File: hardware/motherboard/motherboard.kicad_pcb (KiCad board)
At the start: 2 copper layers, 175 x 127 mm, 82 parts, among them J1 Conn_01x04_Female, J10 Conn_01x02_Female, J11 Conn_01x02_Female, J12 Conn_01x03_Male, J13 Conn_01x03_Male, J14 Conn_01x03_Male, J15 Conn_01x06_Female, J16 Conn_01x02_Female, J2 Conn_01x03_Male, J3 Conn_01x05_Female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

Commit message: version v0.3
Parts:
- removed D10: LED, LED_SMD:LED_1210_3225Metric_Pad1.42x2.65mm_HandSolder
- added J17: Conn_01x03_Male, Connector_PinHeader_2.54mm:PinHeader_1x03_P2.54mm_Vertical, F.Cu at (99.5, 58.6)
- added J18: Conn_01x01_Female, Connector_Wire:SolderWirePad_1x01_Drill2.5mm, F.Cu at (165.5, 37.6)
- added J19: Conn_01x01_Female, Connector_Wire:SolderWirePad_1x01_Drill2.5mm, F.Cu at (121.1, 137.5)
- added Q5: BSS138, Package_TO_SOT_SMD:SOT-23_Handsoldering, F.Cu at (48.0, 105.0)
- added R25: ?, Resistor_SMD:R_1210_3225Metric_Pad1.42x2.65mm_HandSolder, B.Cu at (28.4, 76.5)
- D1, R1, R18, R2, R20, R21, R24, R4: moved to B.Cu
- Q1, Q2, Q3, Q4: moved to F.Cu
- R17, R5: value ? -> 10K; moved to B.Cu
- moved R24 156.7 mm to (28.4, 81.3)
- moved D6 156.7 mm to (28.4, 81.3)
- moved D7 147.8 mm to (28.4, 86.0), turned to 180 degrees
- moved R18 146.8 mm to (28.4, 86.0), turned to 0 degrees
- moved R17 139.0 mm to (48.0, 102.0), turned to 180 degrees
- moved R21 77.3 mm to (28.4, 71.7), turned to 0 degrees
- moved D9 77.2 mm to (28.4, 76.5), turned to 180 degrees
- moved R5 38.6 mm to (48.0, 107.8)
- moved J14 32.7 mm to (92.1, 137.0), turned to 270 degrees
- moved J12 32.2 mm to (92.1, 117.6), turned to 270 degrees
- moved J3 30.0 mm to (123.5, 147.7), turned to 180 degrees
- moved J13 29.4 mm to (92.1, 127.3), turned to 270 degrees
- moved R19 20.4 mm to (66.8, 102.0), turned to 0 degrees
- moved R1 19.0 mm to (103.1, 138.0), turned to 270 degrees
- moved Q1 18.5 mm to (66.8, 105.0), turned to 270 degrees
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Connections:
- D8 pad 1: GND -> Net-(D8-Pad1)
- J3 pad 4: +5V -> +3V3
- J3 pad 5: +3V3 -> +5V
- J4 pad 1: Net-(J4-Pad1) -> Net-(D8-Pad2)
- J5 pad 3: +5V -> Net-(J17-Pad2)
- J5 pad 5: Net-(J5-Pad5) -> Net-(D1-Pad2)
- J7 pad 2: /M1_HA -> +5V
- J7 pad 3: /M2_HA -> /M1_HA
- J7 pad 4: /M3_HA -> /M2_HA
- J7 pad 5: +5V -> /M3_HA
- K2 pad 1: Net-(J4-Pad1) -> Net-(D8-Pad2)
- K2 pad 3: +12V -> Net-(J18-Pad1)
- R1 pad 2: +3V3 -> +5V
- R17 pad 1: Net-(D6-Pad2) -> +3V3
- R17 pad 2: Net-(J8-Pad2) -> /GPIO16
- R18 pad 2: /GPIO13(PWM1) -> /GPIO19(SPI1_MISO)
- R2 pad 2: +5V -> +3V3
- R20 pad 1: Net-(D8-Pad2) -> GND
- R20 pad 2: Net-(J4-Pad1) -> Net-(D8-Pad1)
- R21 pad 1: Net-(D9-Pad2) -> Net-(D5-Pad2)
- R21 pad 2: Net-(J5-Pad2) -> /GPIO11(SPI0_SCK)
- R24 pad 1: Net-(D10-Pad2) -> Net-(D6-Pad2)
- R24 pad 2: Net-(J16-Pad2) -> /GPIO13(PWM1)
- R5 pad 1: Net-(D5-Pad2) -> Net-(J5-Pad4)
- R5 pad 2: /GPIO14(TXD0) -> +5V
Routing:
- net /GPIO13(PWM1): track 180.5 -> 49.9 mm, vias 3 -> 1
- net Net-(J5-Pad4): track 0.00 -> 108.0 mm, vias 0 -> 2
- net +3V3: track 180.7 -> 235.3 mm, vias 3 -> 1
- net +5V: track 451.6 -> 504.2 mm, vias 0 -> 4
- net Net-(D8-Pad2): track 4.00 -> 35.4 mm
- net /M1: track 32.8 -> 61.1 mm
- net /GPIO11(SPI0_SCK): track 40.7 -> 67.8 mm
- net /M2: track 36.6 -> 62.1 mm
- net Net-(J4-Pad1): track 25.1 -> 0.00 mm
- net /GPIO12(PWM0): track 32.5 -> 57.5 mm
- net +12V: track 130.4 -> 155.0 mm, vias 23 -> 0
- net /M3: track 41.9 -> 63.0 mm
- net /GPIO16: track 0.00 -> 17.0 mm, vias 0 -> 1
- net Net-(J5-Pad2): track 111.8 -> 95.3 mm, vias 0 -> 2
- net Net-(J18-Pad1): track 0.00 -> 15.9 mm
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- removed copper zone on B.Cu, net +12V
- removed copper zone on F.Cu, net +12V
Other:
- outline, holes or cut-outs redrawn
- board text added: "Christian Skjerning | 2020 Q3 Stjær Dagli'Brugsens Juletog | v0.3 github.com/slimcdk/sdb-xmas-train"
- board text added: "IO11"
- board text added: "IO12"
- board text added: "IO13"
- board text added: "IO19"
- board text removed: "12V RAIL"
- board text removed: "CHRISTIAN SKJERNING SDB XMAS TRAIN v2 2020 Q3"
- board text removed: "github.com/slimcdk/ sdb-xmas-train"

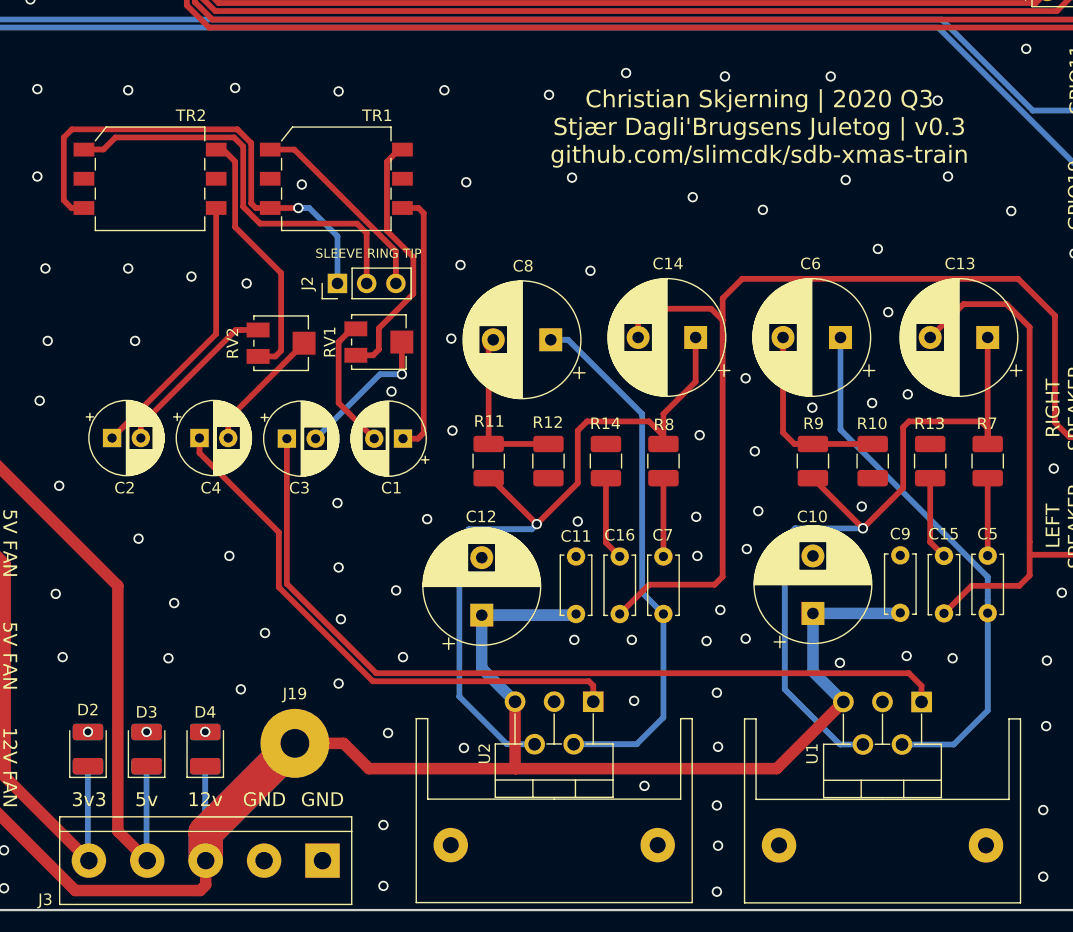
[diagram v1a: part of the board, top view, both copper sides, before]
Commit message: adjusted heatsink
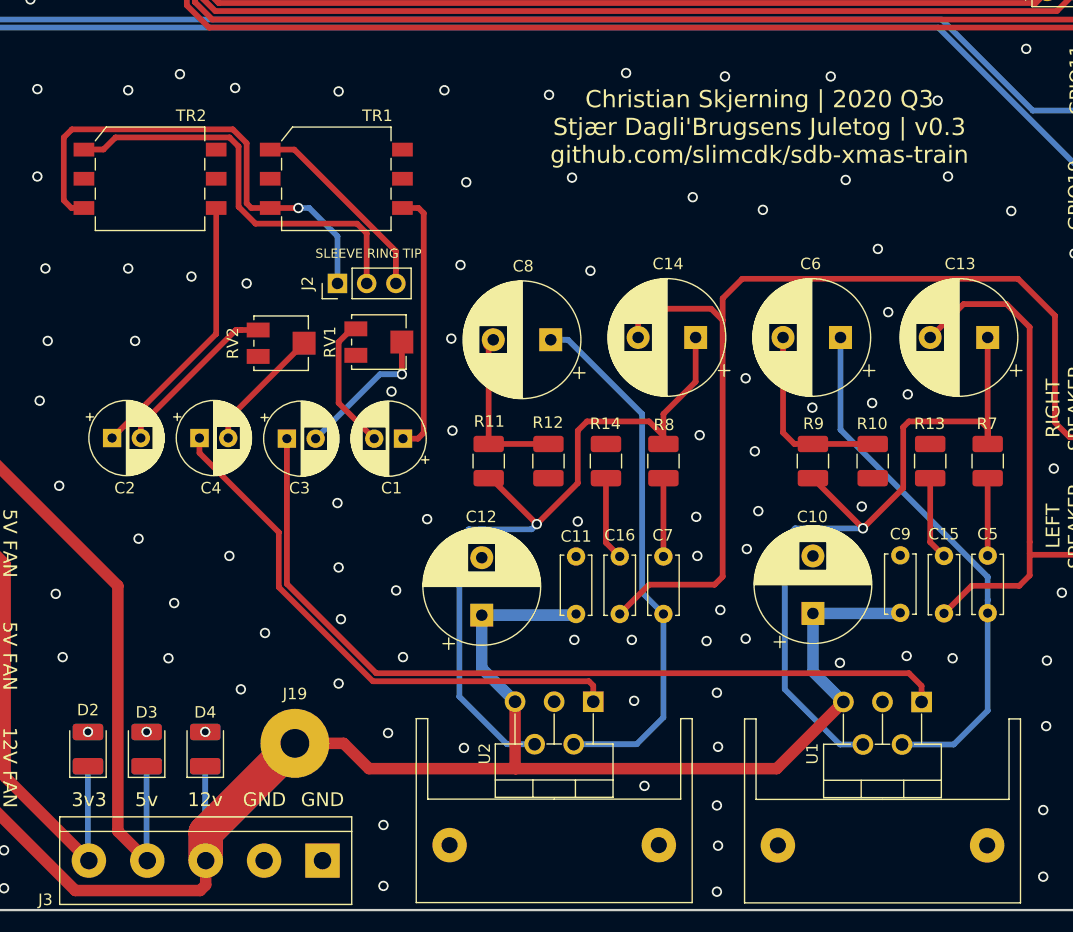
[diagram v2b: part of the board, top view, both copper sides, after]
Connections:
- RV1 pad 3: Net-(RV1-Pad3) -> GND
- RV2 pad 3: Net-(RV2-Pad3) -> GND
- TR1 pad 4: Net-(RV1-Pad3) -> GND
- TR2 pad 4: Net-(RV2-Pad3) -> GND
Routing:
- net Net-(RV1-Pad3): track 22.5 -> 0.00 mm
- net Net-(RV2-Pad3): track 22.1 -> 0.00 mm

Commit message: hardware revision 0.3
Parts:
- removed D1: 1N4148W, Diode_SMD:D_SOD-128
- removed D8: LED, LED_SMD:LED_1210_3225Metric_Pad1.42x2.65mm_HandSolder
- removed K2: SANYOU_SRD_Form_C, Relay_THT:Relay_SPDT_SANYOU_SRD_Series_Form_C
- removed Q1, Q2, Q3, Q4, Q5: BSS138, Package_TO_SOT_SMD:SOT-23_Handsoldering
- removed R15, R23, R3: 10K, Resistor_SMD:R_1210_3225Metric_Pad1.42x2.65mm_HandSolder
- removed R20: ?, Resistor_SMD:R_1210_3225Metric_Pad1.42x2.65mm_HandSolder
- removed the REF** at (172.2, 142.4)
- removed the REF** at (143.7, 142.3)
- added REF**: Unknown_TO220_16x24mm_Heatsink, Local_Heatsink:Unknown_TO220_16x24mm_Heatsink, F.Cu at (171.0, 141.6)
- added REF**: Unknown_TO220_16x24mm_Heatsink, Local_Heatsink:Unknown_TO220_16x24mm_Heatsink, F.Cu at (142.5, 141.6)
- added U3: 74HCT125, Package_DIP:DIP-14_W7.62mm_Socket_LongPads, F.Cu at (98.3, 59.9)
- R17: value 10K -> 5.1K; moved to F.Cu
- R5: moved to F.Cu
- moved R5 92.0 mm to (130.0, 66.2)
- moved J7 88.0 mm to (111.7, 49.5), turned to 180 degrees
- moved R17 84.5 mm to (124.6, 66.2)
- moved J10 74.0 mm to (130.5, 78.7)
- moved J11 66.1 mm to (130.5, 88.9)
- moved J17 25.7 mm to (125.1, 56.1), turned to 0 degrees
- moved R6 22.2 mm to (51.0, 105.7), turned to 270 degrees
- moved J18 21.1 mm to (185.6, 44.0)
- moved RV2 20.7 mm to (100.1, 96.5)
- moved RV1 20.7 mm to (108.6, 96.4)
- moved R19 20.0 mm to (47.1, 105.7), turned to 270 degrees
- moved J16 16.9 mm to (185.6, 73.1)
- moved D5 13.3 mm to (29.1, 85.0), turned to 90 degrees
- moved R21 13.3 mm to (29.1, 85.0), turned to 270 degrees
- moved R16 12.1 mm to (54.9, 105.7), turned to 270 degrees
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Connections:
- J4 pad 1: Net-(D8-Pad2) -> Net-(J18-Pad1)
- J5 pad 2: Net-(J5-Pad2) -> /MOTOR_VR
- J5 pad 5: Net-(D1-Pad2) -> /MOTOR_EL
- R16 pad 1: Net-(J5-Pad2) -> /GPIO12(PWM0)
- R16 pad 2: +5V -> GND
- R17 pad 1: +3V3 -> /GPIO16
- R17 pad 2: /GPIO16 -> Net-(J5-Pad4)
- R18 pad 2: /GPIO19(SPI1_MISO) -> /GPIO12(PWM0)
- R19 pad 1: /GPIO12(PWM0) -> /GPIO21(SPI1_SCK)
- R21 pad 2: /GPIO11(SPI0_SCK) -> /GPIO19(SPI1_MISO)
- R22 pad 1: /GPIO19(SPI1_MISO) -> /GPIO18(GEN1)(PWM0)
- R24 pad 2: /GPIO13(PWM1) -> /GPIO21(SPI1_SCK)
- R25 pad 2: /GPIO12(PWM0) -> /GPIO18(GEN1)(PWM0)
- R5 pad 1: Net-(J5-Pad4) -> /GPIO16
- R5 pad 2: +5V -> GND
- R6 pad 1: Net-(J8-Pad2) -> /GPIO19(SPI1_MISO)
- R6 pad 2: +5V -> GND
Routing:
- net Net-(D1-Pad2): track 190.3 -> 0.00 mm, vias 1 -> 0
- net +5V: track 504.2 -> 328.9 mm, vias 4 -> 0
- net /GPIO18(GEN1)(PWM0): track 0.00 -> 147.7 mm, vias 0 -> 1
- net /GPIO21(SPI1_SCK): track 0.00 -> 116.8 mm, vias 0 -> 1
- net /GPIO16: track 17.0 -> 130.0 mm
- net /M1_HA: track 112.0 -> 7.35 mm
- net Net-(J16-Pad2): track 187.9 -> 84.2 mm, vias 1 -> 0
- net /M2_HA: track 110.9 -> 7.35 mm
- net /M3_HA: track 109.7 -> 7.35 mm
- net Net-(J5-Pad4): track 108.0 -> 6.70 mm, vias 2 -> 0
- net Net-(J5-Pad2): track 95.3 -> 0.00 mm, vias 2 -> 0
- net /GPIO19(SPI1_MISO): track 37.5 -> 116.5 mm
- net Net-(J8-Pad2): track 158.0 -> 85.2 mm, vias 1 -> 0
- net +3V3: track 235.3 -> 163.9 mm, vias 1 -> 0
- net /GPIO11(SPI0_SCK): track 67.8 -> 0.00 mm, vias 1 -> 0
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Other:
- board size 175 x 127 mm -> 165 x 127 mm
- board text added: "GPIO18"
- board text added: "GPIO21"
- board text added: "IO18"
- board text added: "IO21"
- board text added: "L-SPEAK"
- board text added: "R-SPEAK"
- board text added: "TIP RING SLEEVE"
- board text removed: "GPIO11"
- board text removed: "GPIO19"
- board text removed: "IO11"
- board text removed: "IO13"
- board text removed: "LEFT SPEAKER"
- board text removed: "RIGHT SPEAKER"
- board text removed: "SLEEVE RING TIP"

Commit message: hardware v0.3
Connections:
- U3 pad 1: /GPIO19(SPI1_MISO) -> GND
- U3 pad 10: /GPIO21(SPI1_SCK) -> GND
- U3 pad 12: GND -> /GPIO18(GEN1)(PWM0)
- U3 pad 13: /GPIO18(GEN1)(PWM0) -> GND
- U3 pad 2: GND -> /GPIO19(SPI1_MISO)
- U3 pad 4: /GPIO12(PWM0) -> GND
- U3 pad 5: GND -> /GPIO12(PWM0)
- U3 pad 9: GND -> /GPIO21(SPI1_SCK)
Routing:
- net /GPIO18(GEN1)(PWM0): track 147.7 -> 145.2 mm
- net /GPIO19(SPI1_MISO): track 116.5 -> 113.9 mm
- net /GPIO21(SPI1_SCK): track 116.8 -> 114.2 mm
- net /GPIO12(PWM0): track 115.4 -> 113.9 mm
